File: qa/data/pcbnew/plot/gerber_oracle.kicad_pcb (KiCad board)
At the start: 4 copper layers, 60 x 40 mm, 2 parts, among them J1 CONN, U1 SHAPES

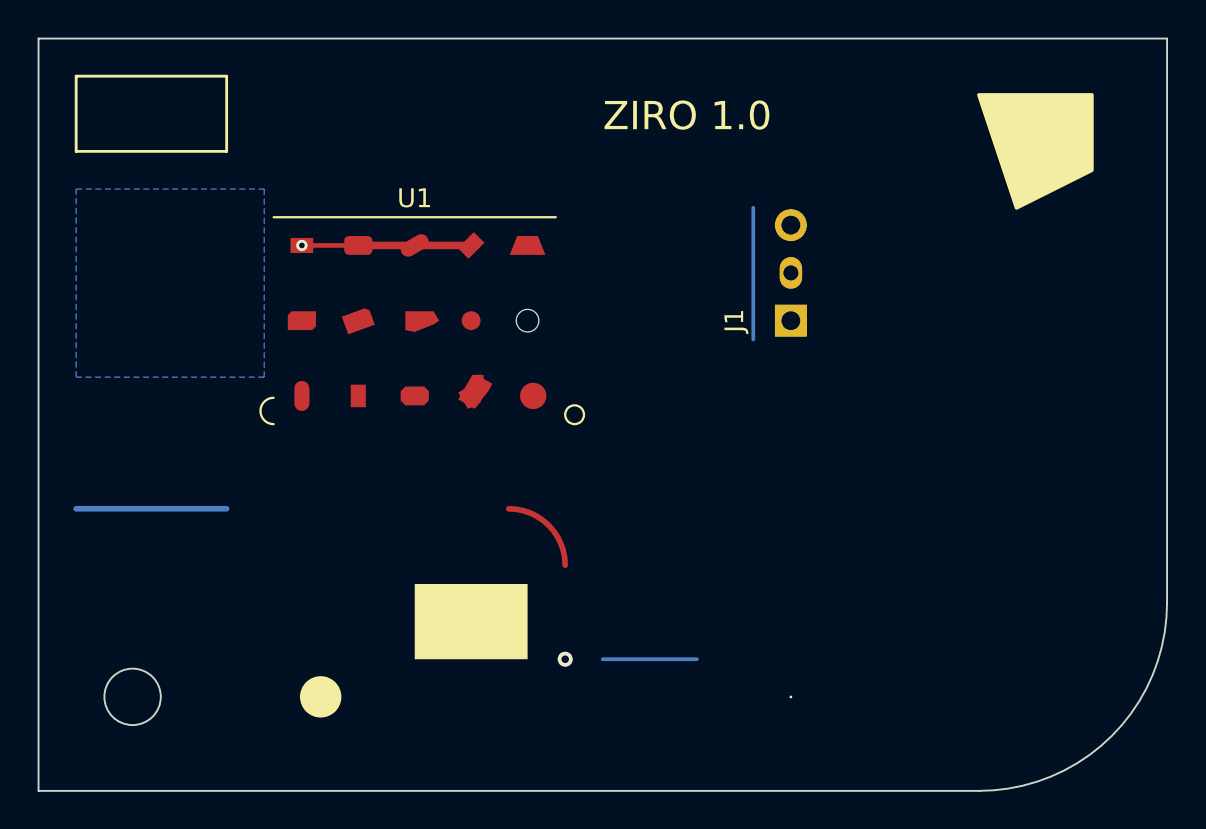
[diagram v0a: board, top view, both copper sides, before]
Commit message: pcbnew/exporters: GENDRILL_WRITER_BASE, EXCELLON_WRITER, GERBER_JOBFILE_WRITER
Replaces the two function writers with KiCad's classes:
gendrill_writer_base.cpp (hole and tool lists, drill spans, file names,
FileFunction, drill maps through the plotters, the drill report),
gendrill_excellon_writer.cpp and gerber_jobfile_writer.cpp (with an
nlohmann-style JSON dump). The plot dialog's Generate Drill Files and its
job file run them.

Pinned against kicad-cli 10.0.6: pcb export drill in seven option sets
(merged / separate, mm / inch, all four zero formats, mirror + minimal
header + routed slots, plot origin, report, Gerber drill maps) byte for
byte but for program and clock, and the .gbrjob beside the gerber oracle.
The oracle board gains oblong holes, blind and buried vias, so the gerber
oracle is regenerated too (still byte-identical).

A blind span ending on B.Cu follows the 10.0.5 source ("-back-in2"),
which 10.0.6 names "-in2-back"; pinned by a unit test.

Co-Authored-By: Claude Opus 5.5 (1M context) <noreply@anthropic.com>
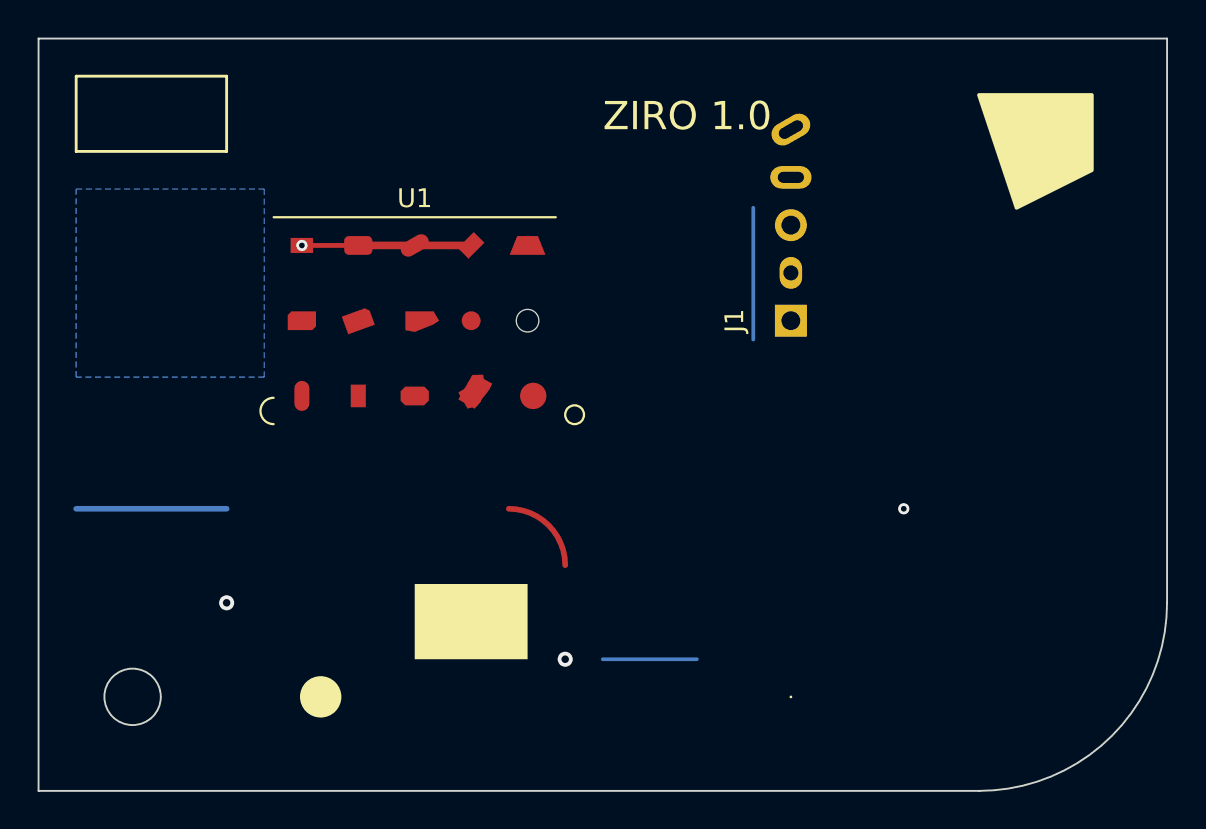
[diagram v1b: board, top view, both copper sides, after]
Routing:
- net VCC: vias 0 -> 2
- net GND: vias 2 -> 3
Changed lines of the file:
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@@
     (pad "1" thru_hole rect (at 0 0 90) (size 1.7 1.7) (drill 1) (layers "*.Cu" "*.Mask") (net 1 "GND"))
     (pad "2" thru_hole oval (at 2.54 0 90) (size 1.7 1.2) (drill 0.8) (layers "*.Cu" "*.Mask") (net 2 "VCC"))
+    (pad "4" thru_hole oval (at 7.62 0 90) (size 1.2 2.2) (drill oval 0.6 1.4) (layers "*.Cu" "*.Mask") (net 2 "VCC"))
+    (pad "5" thru_hole oval (at 10.16 0 30) (size 2.2 1.2) (drill oval 1.4 0.6) (layers "*.Cu" "*.Mask") (net 2 "VCC"))
     (pad "3" thru_hole circle (at 5.08 0 90) (size 1.7 1.7) (drill 1) (layers "*.Cu" "*.Mask") (net 2 "VCC"))
   )
@@
   (via (at 34 26) (size 0.6) (drill 0.3) (layers "F.Cu" "B.Cu") (net 1))
   (via (at 48 48) (size 0.8) (drill 0.4) (layers "F.Cu" "B.Cu") (net 1))
+  (via blind (at 66 40) (size 0.6) (drill 0.3) (layers "F.Cu" "In1.Cu") (net 1))
+  (via buried (at 68 40) (size 0.6) (drill 0.25) (layers "In1.Cu" "In2.Cu") (net 2))
+  (via (at 30 45) (size 0.8) (drill 0.4) (layers "F.Cu" "B.Cu") (net 2))
   (zone (net 1) (net_name "GND") (layer "B.Cu") (hatch edge 0.5)
     (connect_pads (clearance 0.5))
